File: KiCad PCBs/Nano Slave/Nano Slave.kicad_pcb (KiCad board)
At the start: 2 copper layers, 87 x 54.6 mm, 51 parts, among them J1 Screw_Terminal_01x02, J10 AVR-ISP-6, J11 Conn_01x06_Female, J12 Screw_Terminal_01x02, J13 Screw_Terminal_01x02, J14 Screw_Terminal_01x02, J15 Screw_Terminal_01x02, J16 Screw_Terminal_01x02, J2 Screw_Terminal_01x02, J3 Screw_Terminal_01x02, J4 Screw_Terminal_01x02, J5 Screw_Terminal_01x02, J6 Screw_Terminal_01x02, J7 Screw_Terminal_01x02, J8 Screw_Terminal_01x02, J9 Screw_Terminal_01x02, SW1 SW_DIP_x02, SW2 SW_DIP_x02, SW3 SW_MEC_5E, U1 ATmega328P-AU, U2 MAX487ESA+T, U3 ULN2003A, U4 MAX487CPA+, U5 AMS1117-5.0, Y1 Crystal_GND24

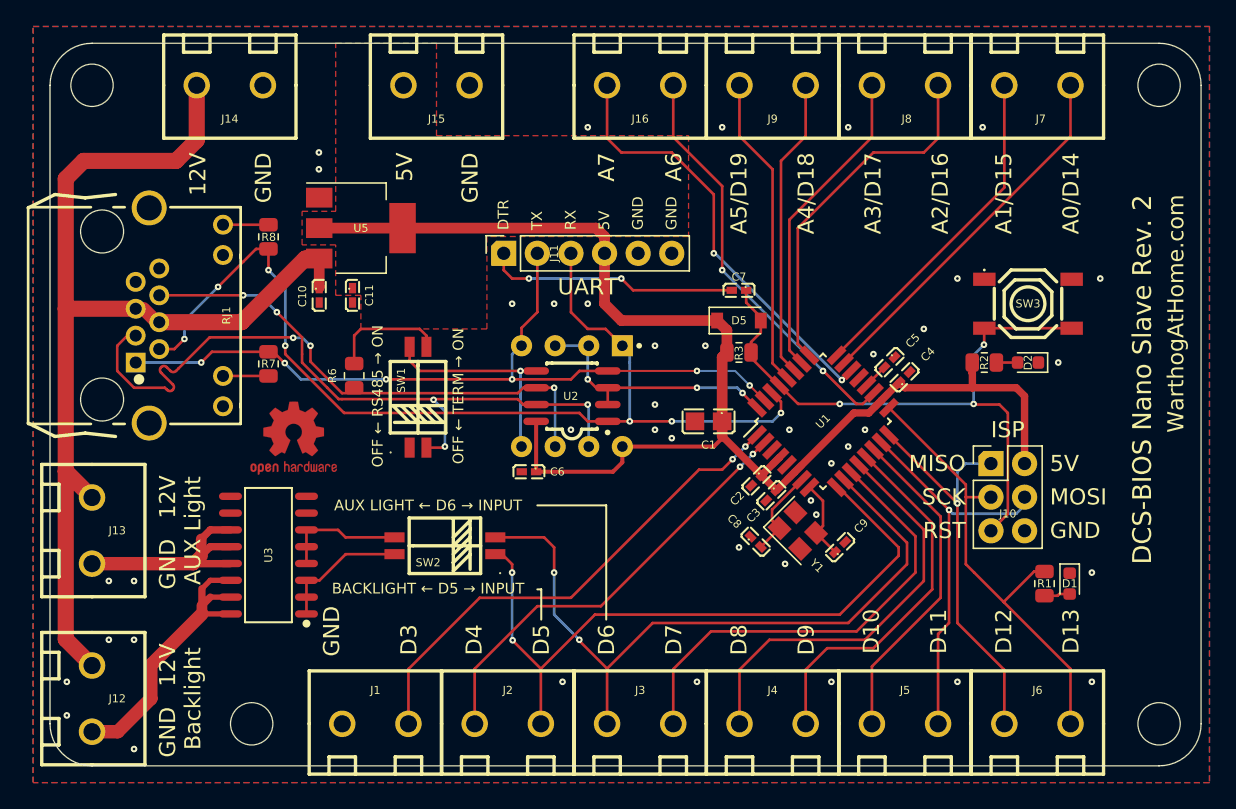
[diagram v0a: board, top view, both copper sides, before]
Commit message: Added measurements to silkscreen
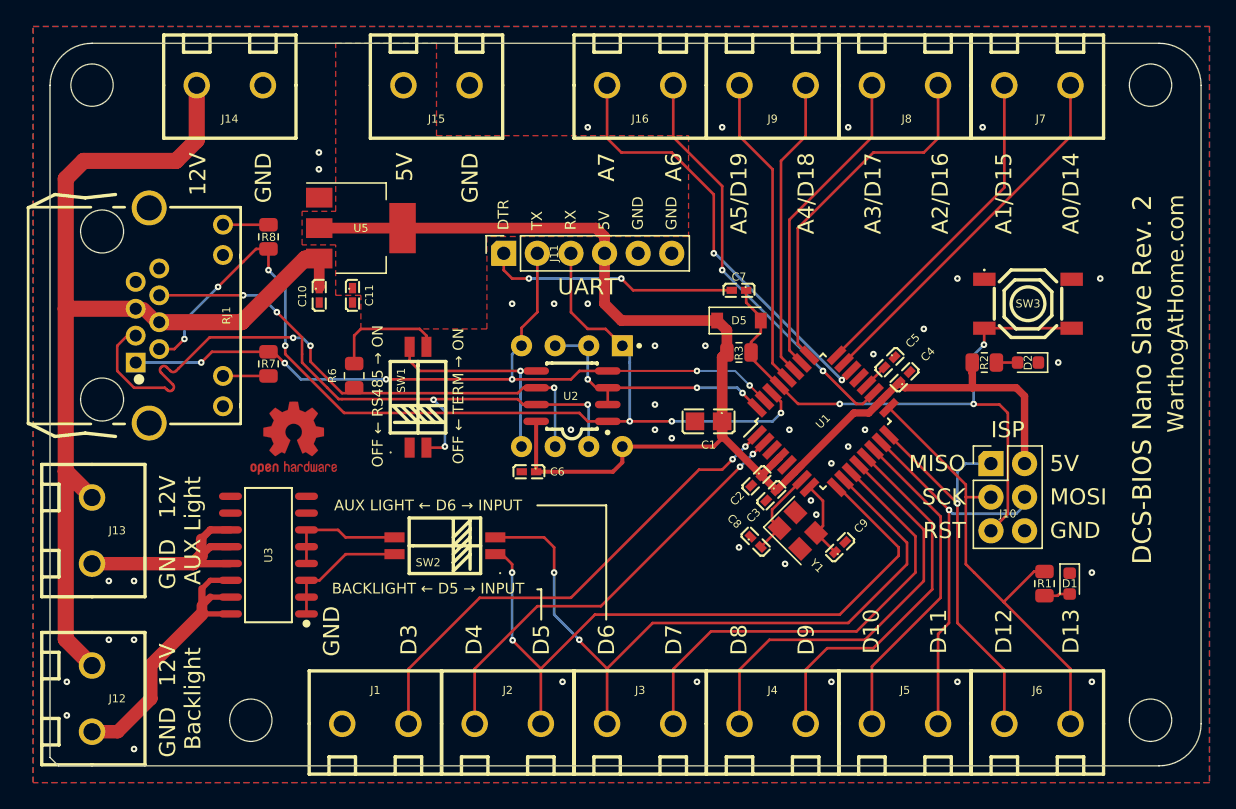
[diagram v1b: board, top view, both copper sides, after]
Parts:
- R1, R2: value 1K -> 1.5K
- moved H4 0.70 mm to (185.4, 128.0)
- moved H2 0.65 mm to (185.4, 80.0)
- moved H3 0.28 mm to (117.4, 128.0)
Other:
- outline, holes or cut-outs redrawn
- board text added: "48MM →"
- board text added: "80MM →"
- board text added: "M3"
- board text added: "← 68MM"
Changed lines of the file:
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@@
   )
   (footprint "MountingHole:MountingHole_3.2mm_M3" (layer "F.Cu")
-    (at 186.055 128.27)
+    (at 185.41 128)
     (descr "Mounting Hole 3.2mm, no annular, M3")
     (tags "mounting hole 3.2mm no annular m3")
@@
     (descr "Resistor SMD 0805 (2012 Metric), square (rectangular) end terminal, IPC_7351 nominal, (Body size source: IPC-SM-782 page 72, https://www.pcb-3d.com/wordpress/wp-content/uploads/ipc-sm-782a_amendment_1_and_2.pdf), generated with kicad-footprint-generator")
     (tags "resistor")
-    (property "LCSC" "C17513")
+    (property "LCSC" "C4310")
     (property "Sheetfile" "Nano Slave.kicad_sch")
     (property "Sheetname" "")
@@
       (effects (font (size 0.6096 0.6096) (thickness 0.1016)))
     )
-    (fp_text value "1K" (at 0 1.65) (layer "F.Fab")
+    (fp_text value "1.5K" (at 0 1.65) (layer "F.Fab")
       (effects (font (size 1 1) (thickness 0.15)))
     )
@@
   )
   (footprint "MountingHole:MountingHole_3.2mm_M3" (layer "F.Cu")
-    (at 117.475 128.27)
+    (at 117.41 128)
     (descr "Mounting Hole 3.2mm, no annular, M3")
     (tags "mounting hole 3.2mm no annular m3")
@@
   )
   (footprint "MountingHole:MountingHole_3.2mm_M3" (layer "F.Cu")
-    (at 105.41 80.01)
+    (at 105.41 80)
     (descr "Mounting Hole 3.2mm, no annular, M3")
     (tags "mounting hole 3.2mm no annular m3")
@@
     (descr "Resistor SMD 0805 (2012 Metric), square (rectangular) end terminal, IPC_7351 nominal, (Body size source: IPC-SM-782 page 72, https://www.pcb-3d.com/wordpress/wp-content/uploads/ipc-sm-782a_amendment_1_and_2.pdf), generated with kicad-footprint-generator")
     (tags "resistor")
-    (property "LCSC" "C17513")
+    (property "LCSC" "C4310")
     (property "Sheetfile" "Nano Slave.kicad_sch")
     (property "Sheetname" "")
@@
       (effects (font (size 0.6096 0.6096) (thickness 0.1016)))
     )
-    (fp_text value "1K" (at 0 1.65 90) (layer "F.Fab")
+    (fp_text value "1.5K" (at 0 1.65 90) (layer "F.Fab")
       (effects (font (size 1 1) (thickness 0.15)))
     )
@@
   )
   (footprint "MountingHole:MountingHole_3.2mm_M3" (layer "F.Cu")
-    (at 186.055 80.01)
+    (at 185.41 80)
     (descr "Mounting Hole 3.2mm, no annular, M3")
     (tags "mounting hole 3.2mm no annular m3")
@@
   (gr_line (start 139.361704 118.11) (end 139.065 118.11) (layer "F.SilkS") (width 0.1524))
   (gr_line (start 144.272 111.76) (end 139.065 111.76) (layer "F.SilkS") (width 0.1524))
-  (gr_line (start 186.055 131.445) (end 105.41 131.445) (layer "Edge.Cuts") (width 0.1))
-  (gr_arc (start 105.41 131.445) (mid 103.164936 130.515064) (end 102.235 128.27) (layer "Edge.Cuts") (width 0.1))
+  (gr_line (start 186.055 131.445) (end 102.87 131.445) (layer "Edge.Cuts") (width 0.1))
   (gr_line (start 105.41 76.835) (end 186.055 76.835) (layer "Edge.Cuts") (width 0.1))
   (gr_arc (start 186.055 76.835) (mid 188.300064 77.764936) (end 189.23 80.01) (layer "Edge.Cuts") (width 0.1))
   (gr_arc (start 102.235 80.01) (mid 103.164936 77.764936) (end 105.41 76.835) (layer "Edge.Cuts") (width 0.1))
   (gr_line (start 189.23 80.01) (end 189.23 128.27) (layer "Edge.Cuts") (width 0.1))
+  (gr_line (start 102.235 130.81) (end 102.87 131.445) (layer "Edge.Cuts") (width 0.1))
   (gr_arc (start 189.23 128.27) (mid 188.300064 130.515064) (end 186.055 131.445) (layer "Edge.Cuts") (width 0.1))
-  (gr_line (start 102.235 128.27) (end 102.235 80.01) (layer "Edge.Cuts") (width 0.1))
+  (gr_line (start 102.235 130.81) (end 102.235 80.01) (layer "Edge.Cuts") (width 0.1))
+  (gr_text "48MM →" (at 185.42 120.65 270) (layer "B.SilkS")
+    (effects (font (size 1.2192 1.2192) (thickness 0.1524)) (justify mirror))
+  )
+  (gr_text "80MM →" (at 184.15 83.82) (layer "B.SilkS")
+    (effects (font (size 1.2192 1.2192) (thickness 0.1524)) (justify mirror))
+  )
+  (gr_text "← 68MM" (at 118.11 123.825) (layer "B.SilkS")
+    (effects (font (size 1.2192 1.2192) (thickness 0.1524)) (justify mirror))
+  )
+  (gr_text "M3" (at 105.41 83.82) (layer "B.SilkS")
+    (effects (font (size 1.2192 1.2192) (thickness 0.1524)) (justify mirror))
+  )
   (gr_text "BRRRRRRRRT" (at 145.669 104.521 15) (layer "B.SilkS")
     (effects (font (size 6.5024 6.5024) (thickness 0.8128)) (justify mirror))

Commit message: Fixed PCB size
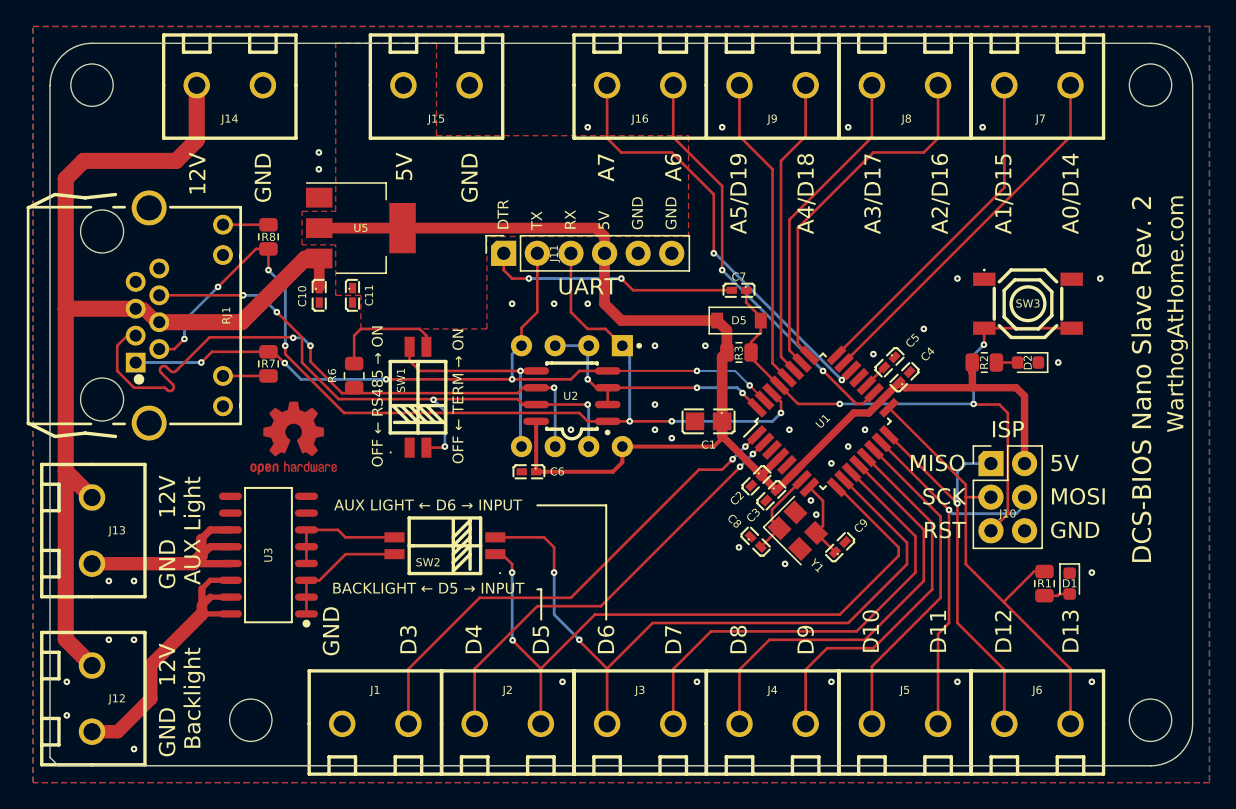
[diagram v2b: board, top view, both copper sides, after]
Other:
- board size 87 x 54.6 mm -> 86.4 x 54.6 mm
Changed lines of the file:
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@@
   (gr_line (start 139.361704 118.11) (end 139.065 118.11) (layer "F.SilkS") (width 0.1524))
   (gr_line (start 144.272 111.76) (end 139.065 111.76) (layer "F.SilkS") (width 0.1524))
-  (gr_line (start 186.055 131.445) (end 102.87 131.445) (layer "Edge.Cuts") (width 0.1))
-  (gr_line (start 105.41 76.835) (end 186.055 76.835) (layer "Edge.Cuts") (width 0.1))
-  (gr_arc (start 186.055 76.835) (mid 188.300064 77.764936) (end 189.23 80.01) (layer "Edge.Cuts") (width 0.1))
+  (gr_line (start 185.42 131.445) (end 102.87 131.445) (layer "Edge.Cuts") (width 0.1))
+  (gr_line (start 105.41 76.835) (end 185.42 76.835) (layer "Edge.Cuts") (width 0.1))
+  (gr_arc (start 185.42 76.835) (mid 187.665064 77.764936) (end 188.595 80.01) (layer "Edge.Cuts") (width 0.1))
   (gr_arc (start 102.235 80.01) (mid 103.164936 77.764936) (end 105.41 76.835) (layer "Edge.Cuts") (width 0.1))
-  (gr_line (start 189.23 80.01) (end 189.23 128.27) (layer "Edge.Cuts") (width 0.1))
+  (gr_line (start 188.595 80.01) (end 188.595 128.27) (layer "Edge.Cuts") (width 0.1))
   (gr_line (start 102.235 130.81) (end 102.87 131.445) (layer "Edge.Cuts") (width 0.1))
-  (gr_arc (start 189.23 128.27) (mid 188.300064 130.515064) (end 186.055 131.445) (layer "Edge.Cuts") (width 0.1))
+  (gr_arc (start 188.595 128.27) (mid 187.665064 130.515064) (end 185.42 131.445) (layer "Edge.Cuts") (width 0.1))
   (gr_line (start 102.235 130.81) (end 102.235 80.01) (layer "Edge.Cuts") (width 0.1))
   (gr_text "48MM →" (at 185.42 120.65 270) (layer "B.SilkS")

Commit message: Cleaned up routing on Nano Shield
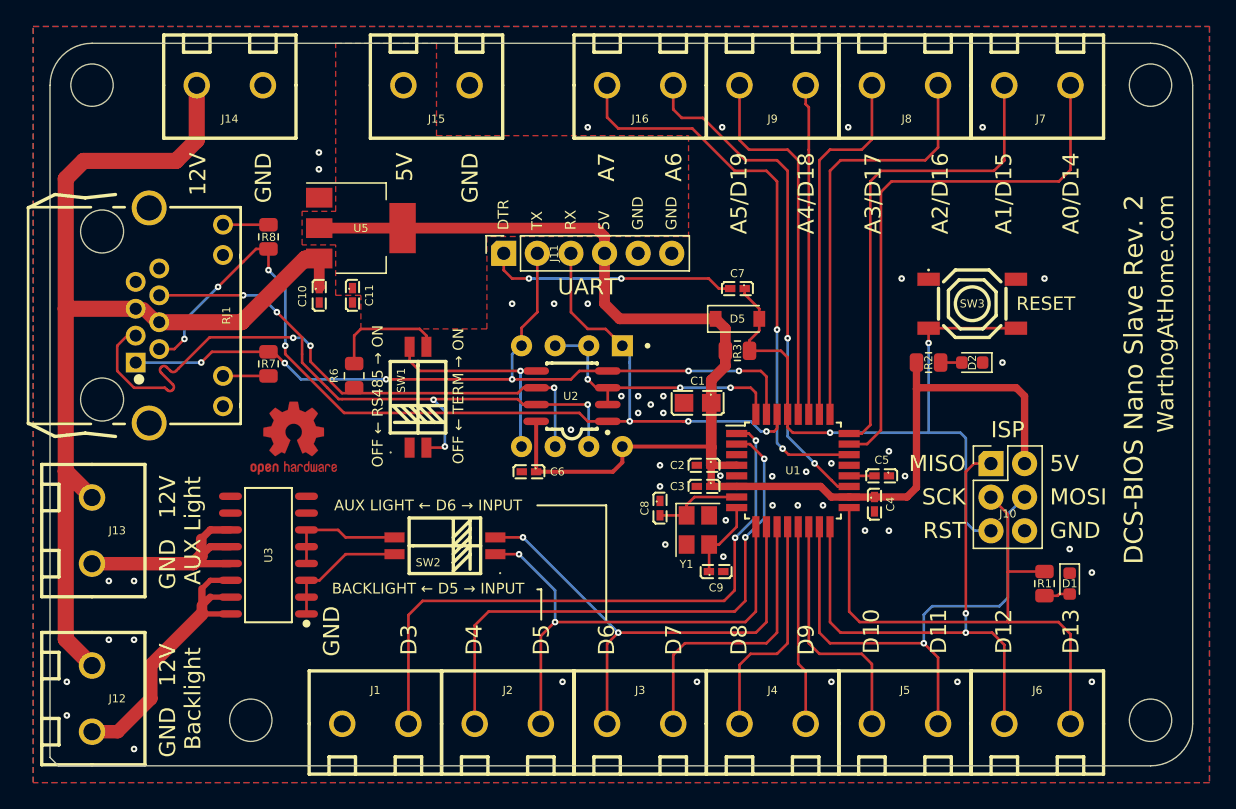
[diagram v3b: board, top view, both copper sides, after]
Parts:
- moved C4 9.86 mm to (164.5, 111.7), turned to -90 degrees
- moved C9 9.55 mm to (152.6, 116.8), turned to 0 degrees
- moved C5 8.60 mm to (165.1, 109.5), turned to 180 degrees
- moved C8 7.67 mm to (148.3, 112.0), turned to -90 degrees
- moved Y1 7.55 mm to (151.2, 113.6), turned to -90 degrees
- moved C3 5.13 mm to (151.7, 110.3), turned to 180 degrees
- moved U1 4.36 mm to (158.4, 109.1), turned to 0 degrees
- moved R2 4.21 mm to (168.6, 101.0)
- moved D2 4.21 mm to (171.9, 101.0)
- moved SW3 4.21 mm to (171.9, 96.5)
- moved C2 4.12 mm to (151.7, 108.7), turned to 180 degrees
- moved C1 1.62 mm to (151.2, 104.0)
- moved C7 0.17 mm to (154.2, 95.4)
- moved D5 0.17 mm to (154.2, 97.7)
- moved R3 0.17 mm to (154.2, 100.1)
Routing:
- net D6: track 54.0 -> 38.2 mm
- net D5: track 52.3 -> 38.1 mm
- net A0: track 28.1 -> 42.2 mm
- net D8: track 31.6 -> 17.6 mm
- net D7: track 35.0 -> 21.8 mm
- net D9: track 28.2 -> 15.1 mm
- net A1: track 25.7 -> 36.7 mm
- net D12: track 30.6 -> 41.4 mm, vias 1 -> 2
- net A7: track 33.0 -> 42.9 mm
- net D11: track 30.4 -> 39.9 mm
- net D3: track 37.8 -> 47.3 mm
- net D4: track 33.2 -> 42.6 mm
- net D13: track 35.5 -> 44.8 mm
- net A6: track 31.5 -> 38.7 mm
- net +5V: track 102.1 -> 108.8 mm
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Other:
- board text added: "RESET"
